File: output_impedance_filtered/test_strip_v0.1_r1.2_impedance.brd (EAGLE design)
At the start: 121.9 x 176.5 mm, 0 parts

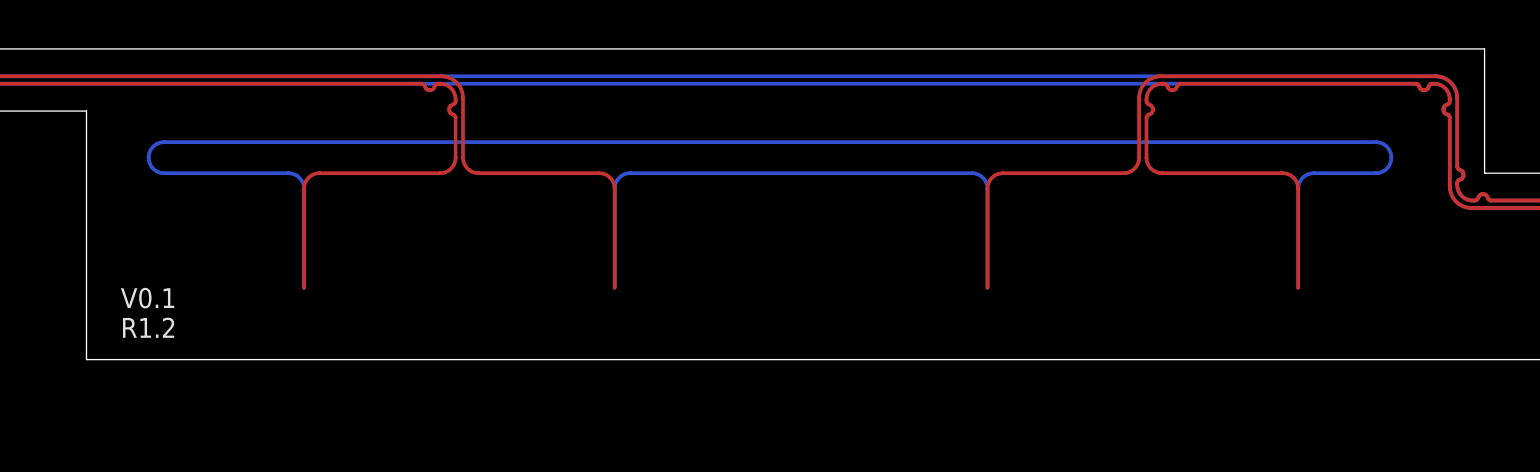
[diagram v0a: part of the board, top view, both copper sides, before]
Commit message: updated impedance filtered output brds
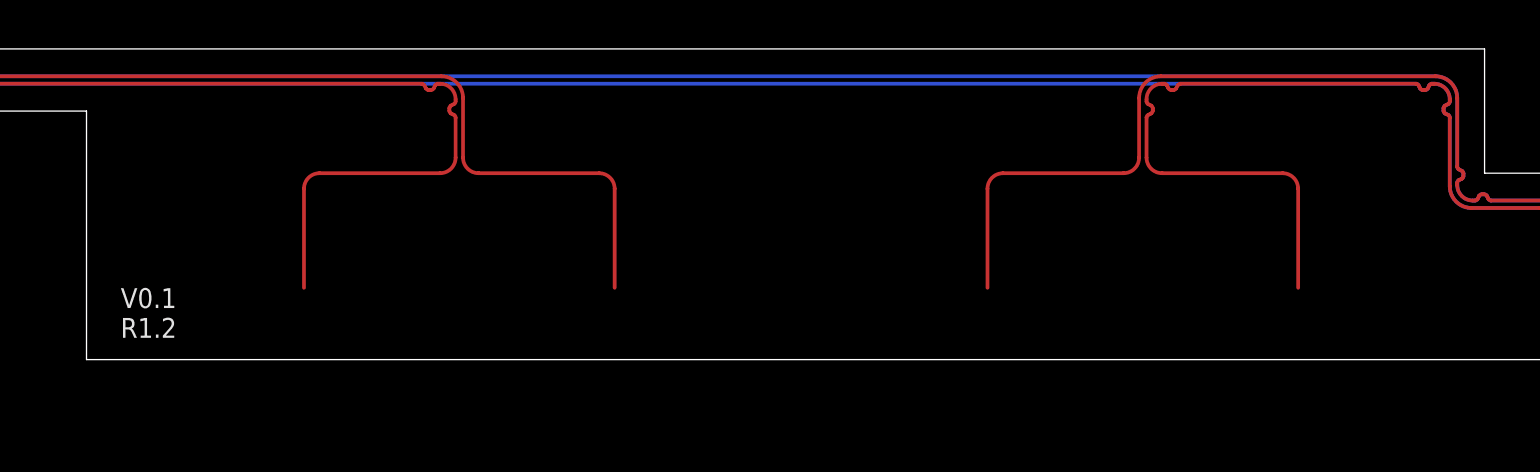
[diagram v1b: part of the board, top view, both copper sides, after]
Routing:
- net SIGB_N: track 70.6 -> 0.00 mm
- net SIGB_P: track 23.9 -> 0.00 mm
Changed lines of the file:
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@@
 <wire x1="27.4574" y1="3.3274" x2="27.4574" y2="3.414009375" width="0.1524" layer="16"/>
-</signal>
-<signal name="SIGB_P" class="1">
-<wire x1="8.255" y1="-0.875" x2="8.255" y2="3.175" width="0.1524" layer="16"/>
-<wire x1="8.255" y1="3.175" x2="7.62" y2="3.81" width="0.1524" layer="16" curve="90"/>
-<wire x1="7.62" y1="3.81" x2="-6.35" y2="3.81" width="0.1524" layer="16"/>
-<wire x1="-6.35" y1="3.81" x2="-6.985" y2="3.175" width="0.1524" layer="16" curve="90"/>
-<wire x1="-6.985" y1="3.175" x2="-6.985" y2="-0.875" width="0.1524" layer="16"/>
-</signal>
-<signal name="SIGB_N" class="1">
-<wire x1="-19.685" y1="-0.875" x2="-19.685" y2="3.175" width="0.1524" layer="16"/>
-<wire x1="-19.685" y1="3.175" x2="-20.32" y2="3.81" width="0.1524" layer="16" curve="90"/>
-<wire x1="-20.32" y1="3.81" x2="-25.4" y2="3.81" width="0.1524" layer="16"/>
-<wire x1="-25.4" y1="3.81" x2="-26.035" y2="4.445" width="0.1524" layer="16" curve="-90"/>
-<wire x1="-26.035" y1="4.445" x2="-25.4" y2="5.08" width="0.1524" layer="16" curve="-90"/>
-<wire x1="24.13" y1="5.08" x2="-25.4" y2="5.08" width="0.1524" layer="16"/>
-<wire x1="24.13" y1="5.08" x2="24.765" y2="4.445" width="0.1524" layer="16" curve="-90"/>
-<wire x1="24.765" y1="4.445" x2="24.13" y2="3.81" width="0.1524" layer="16" curve="-90"/>
-<wire x1="24.13" y1="3.81" x2="21.59" y2="3.81" width="0.1524" layer="16"/>
-<wire x1="21.59" y1="3.81" x2="20.955" y2="3.175" width="0.1524" layer="16" curve="90"/>
-<wire x1="20.955" y1="3.175" x2="20.955" y2="-0.875" width="0.1524" layer="16"/>
 </signal>
 </signals>
